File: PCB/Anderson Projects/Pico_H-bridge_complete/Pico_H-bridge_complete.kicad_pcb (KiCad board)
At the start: 4 copper layers, 103.4 x 65.5 mm, 85 parts, among them J1 Screw_Terminal_01x10, J2 Motor Connector, J3 Screw_Terminal_01x02, Q1 AO3400A, Q2 AO3400A, Q3 DMP3130LQ-7, Q4 DMP3130LQ-7, Q5 MMBT3904, Q6 MMBT3904, SW1 SW_DIP_x01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

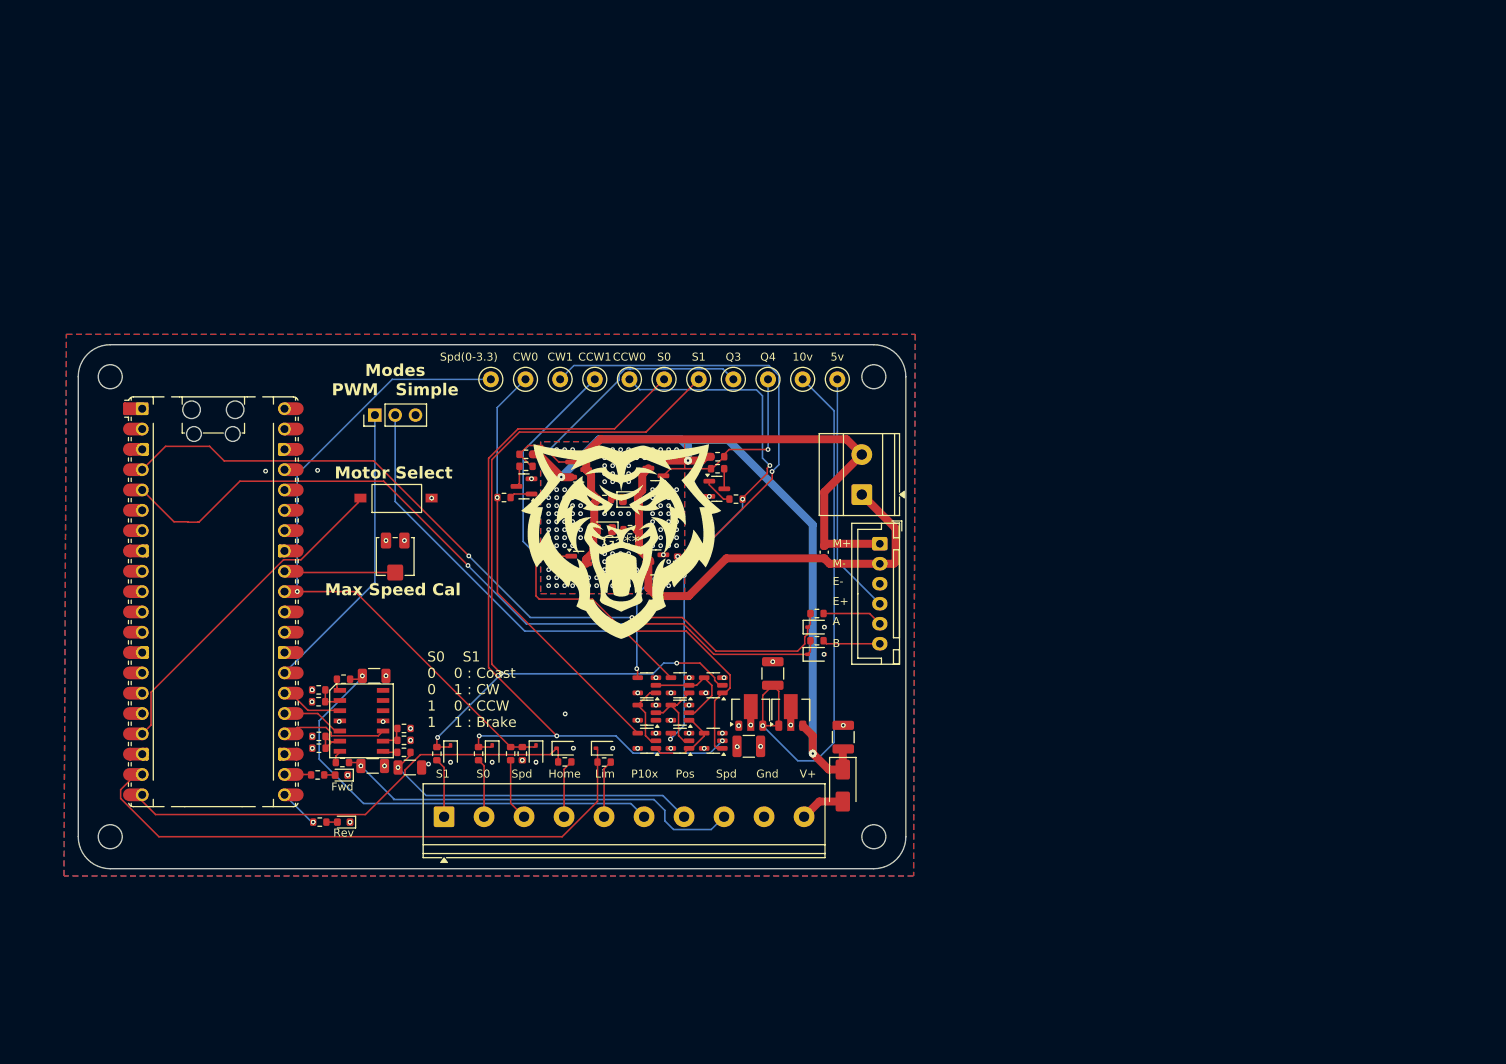
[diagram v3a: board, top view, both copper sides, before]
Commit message: Final Board version prior to testing motor with pulleys. This version would not turn the motor when connected to a generator. The Vgs values for Mosfets needed increased to 10v. Other improvements to make include removing braking functionality to simplify control to Fwd/Rev vice S0/S1.
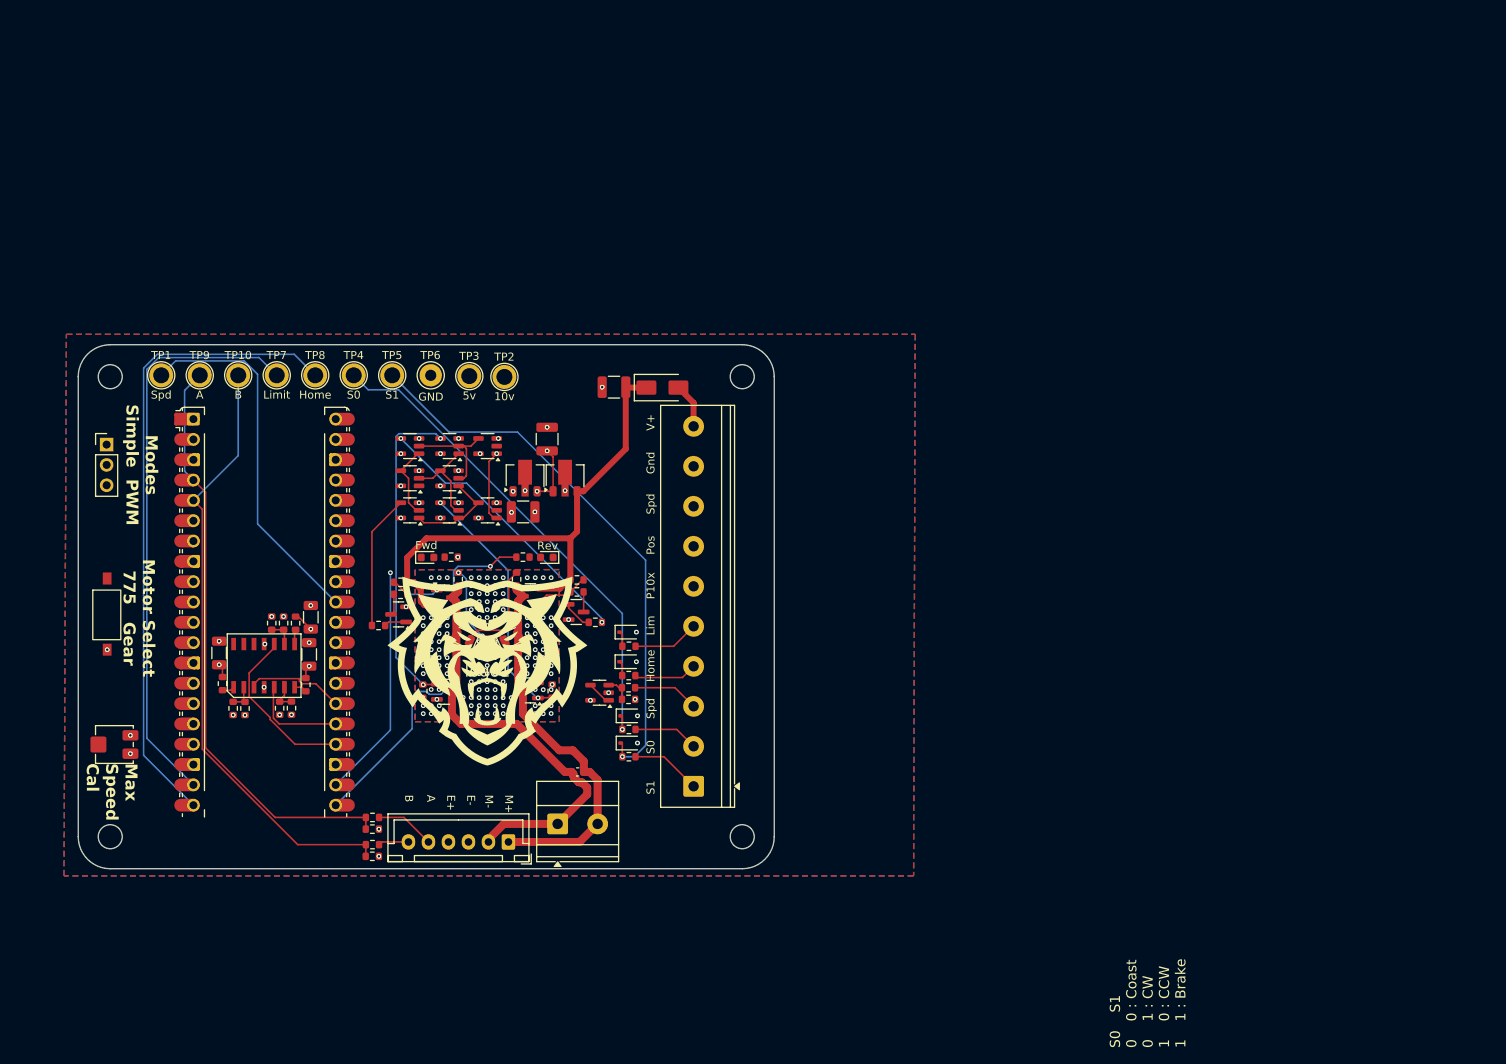
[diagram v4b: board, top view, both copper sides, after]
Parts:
- removed D11, D12, D13, D16, D17: 3.3v, Diode_SMD:D_SOD-323
- removed G***: LOGO, CustomBPA:Bengal_25_25
- removed G***: LOGO, CustomBPA:Bengal_50_50
- removed TP11: CCW1, TestPoint:TestPoint_Loop_D2.50mm_Drill1.0mm
- added D6: 3.3v, Diode_SMD:D_SOD-323, F.Cu at (151.7, 94.6)
- added D7: 3.3v, Diode_SMD:D_SOD-323, F.Cu at (151.7, 90.9)
- added R20: 3.3kΩ, Resistor_SMD:R_0603_1608Metric, F.Cu at (119.8, 119.0)
- added R21: 3.3kΩ, Resistor_SMD:R_0603_1608Metric, F.Cu at (119.8, 115.5)
- added U11: MCP6001R, Package_TO_SOT_SMD:SOT-23-5, F.Cu at (148.2, 98.5)
- added logo1: LOGO, CustomBPA:Bengal_25_25(negative), F.Cu at (134.1, 95.8)
- D1: value LED -> LED_R
- D14, D15: value 3.3v -> 5.1V
- D2: value LED -> LED_W
- D3, D4: value LED -> LED_G
- R10, R4, R6, R8: value 10k -> 3.9k
- R3, R5: value 10k -> 1.8kΩ
- R7, R9: value 1k -> 2.7k
- RV1: value 10k -> 10k pot
- TP1: value Spd(0-3.3) -> Spd; footprint TestPoint:TestPoint_Loop_D2.50mm_Drill1.0mm -> TestPoint:TestPoint_Plated_Hole_D2.0mm
- TP10: value CW0 -> B; footprint TestPoint:TestPoint_Loop_D2.50mm_Drill1.0mm -> TestPoint:TestPoint_Plated_Hole_D2.0mm
- TP2, TP3, TP4, TP5: footprint TestPoint:TestPoint_Loop_D2.50mm_Drill1.0mm -> TestPoint:TestPoint_Plated_Hole_D2.0mm
- TP6: value Q3 -> GND; footprint TestPoint:TestPoint_Loop_D2.50mm_Drill1.0mm -> TestPoint:TestPoint_Loop_D2.60mm_Drill1.4mm_Beaded
- TP7: value Q4 -> Limit; footprint TestPoint:TestPoint_Loop_D2.50mm_Drill1.0mm -> TestPoint:TestPoint_Plated_Hole_D2.0mm
- TP8: value CCW0 -> Home; footprint TestPoint:TestPoint_Loop_D2.50mm_Drill1.0mm -> TestPoint:TestPoint_Plated_Hole_D2.0mm
- TP9: value CW1 -> A; footprint TestPoint:TestPoint_Loop_D2.50mm_Drill1.0mm -> TestPoint:TestPoint_Plated_Hole_D2.0mm
- moved TP7 61.4 mm to (107.8, 58.8)
- moved R3 61.1 mm to (119.8, 114.1)
- moved R5 61.1 mm to (119.8, 117.5)
- moved J2 59.5 mm to (136.8, 117.2), turned to 180 degrees
- moved J3 56.0 mm to (142.9, 114.9), turned to 0 degrees
- moved D5 54.6 mm to (156.0, 60.4), turned to 0 degrees
- moved C4 52.3 mm to (150.0, 60.3), turned to 180 degrees
- moved TP3 46.0 mm to (131.9, 58.9)
- moved TP9 45.1 mm to (98.2, 58.8)
- moved RV1 42.2 mm to (87.5, 105.0), turned to -90 degrees
- moved U3 42.1 mm to (124.5, 67.7)
- moved R1 41.7 mm to (138.6, 81.6)
- moved D1 41.7 mm to (141.6, 81.6)
- moved U10 41.7 mm to (124.5, 71.7)
- moved U12 41.5 mm to (129.4, 67.7)
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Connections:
- C5 pad 1: M+ -> M-
- C5 pad 2: M- -> M+
- D3 pad 2: M+ -> M-
- D4 pad 2: M- -> M+
- Q1 pad 3: M+ -> M-
- Q2 pad 3: M- -> M+
- Q3 pad 3: M+ -> M-
- Q4 pad 3: M- -> M+
- R24 pad 1: Net-(J1-Pin_3) -> GND
- R24 pad 2: Speed_set -> Net-(U11-+)
- R25 pad 1: Speed_set -> Net-(U11-+)
- R25 pad 2: GND -> Net-(J1-Pin_3)
- R7 pad 2: M+ -> M-
- R9 pad 1: Net-(D3-K) -> M+
- R9 pad 2: M- -> Net-(D3-K)
- TP10 pad 1: /H-Bridge/CW0 -> B
- TP6 pad 1: Net-(Q3-G) -> GND
- TP7 pad 1: Net-(Q4-G) -> Limit Switch
- TP8 pad 1: /H-Bridge/CCW0 -> Home
- TP9 pad 1: /H-Bridge/CW1 -> A
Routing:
- net +10V: track 133.2 -> 64.0 mm, vias 2 -> 3
- net /H-Bridge/CW1: track 83.3 -> 31.4 mm, vias 3 -> 2
- net Net-(U1-GPIO13): track 41.8 -> 0.00 mm
- net Net-(U1-GPIO16): track 4.64 -> 46.1 mm
- net S0: track 99.4 -> 62.2 mm, vias 3 -> 1
- net Speed_set PWM: track 36.9 -> 0.00 mm
- net /H-Bridge/CW0: track 53.0 -> 16.8 mm, vias 1 -> 0
- net Net-(U1-GPIO17): track 2.55 -> 38.6 mm, vias 0 -> 2
- net Speed_set: track 82.5 -> 49.1 mm, vias 1 -> 0
- net Net-(Q3-G): track 38.4 -> 6.22 mm, vias 1 -> 2
- net S1: track 101.1 -> 69.7 mm, vias 3 -> 1
- net +Vsup: track 92.6 -> 64.8 mm, vias 3 -> 0
- net /H-Bridge/CCW0: track 61.6 -> 34.9 mm, vias 3 -> 2
- net +5V: track 30.3 -> 56.5 mm
- net A: track 99.1 -> 73.5 mm, vias 2 -> 0
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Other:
- board size 103.4 x 65.5 mm -> 87 x 65.5 mm
- board text added: "Modes Simple PWM"
- board text added: "Motor Select 775 Gear"
- board text added: "PLC Motor Interface Board Anderson - rev1 July 2025"
- board text removed: "Modes PWM Simple"
- board text removed: "Motor Select"
- board text removed: "PLC Motor Interface Board Anderson - rev0 June 2025"

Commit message: Gerber files for Pico_H-bridge_complete v1 generated
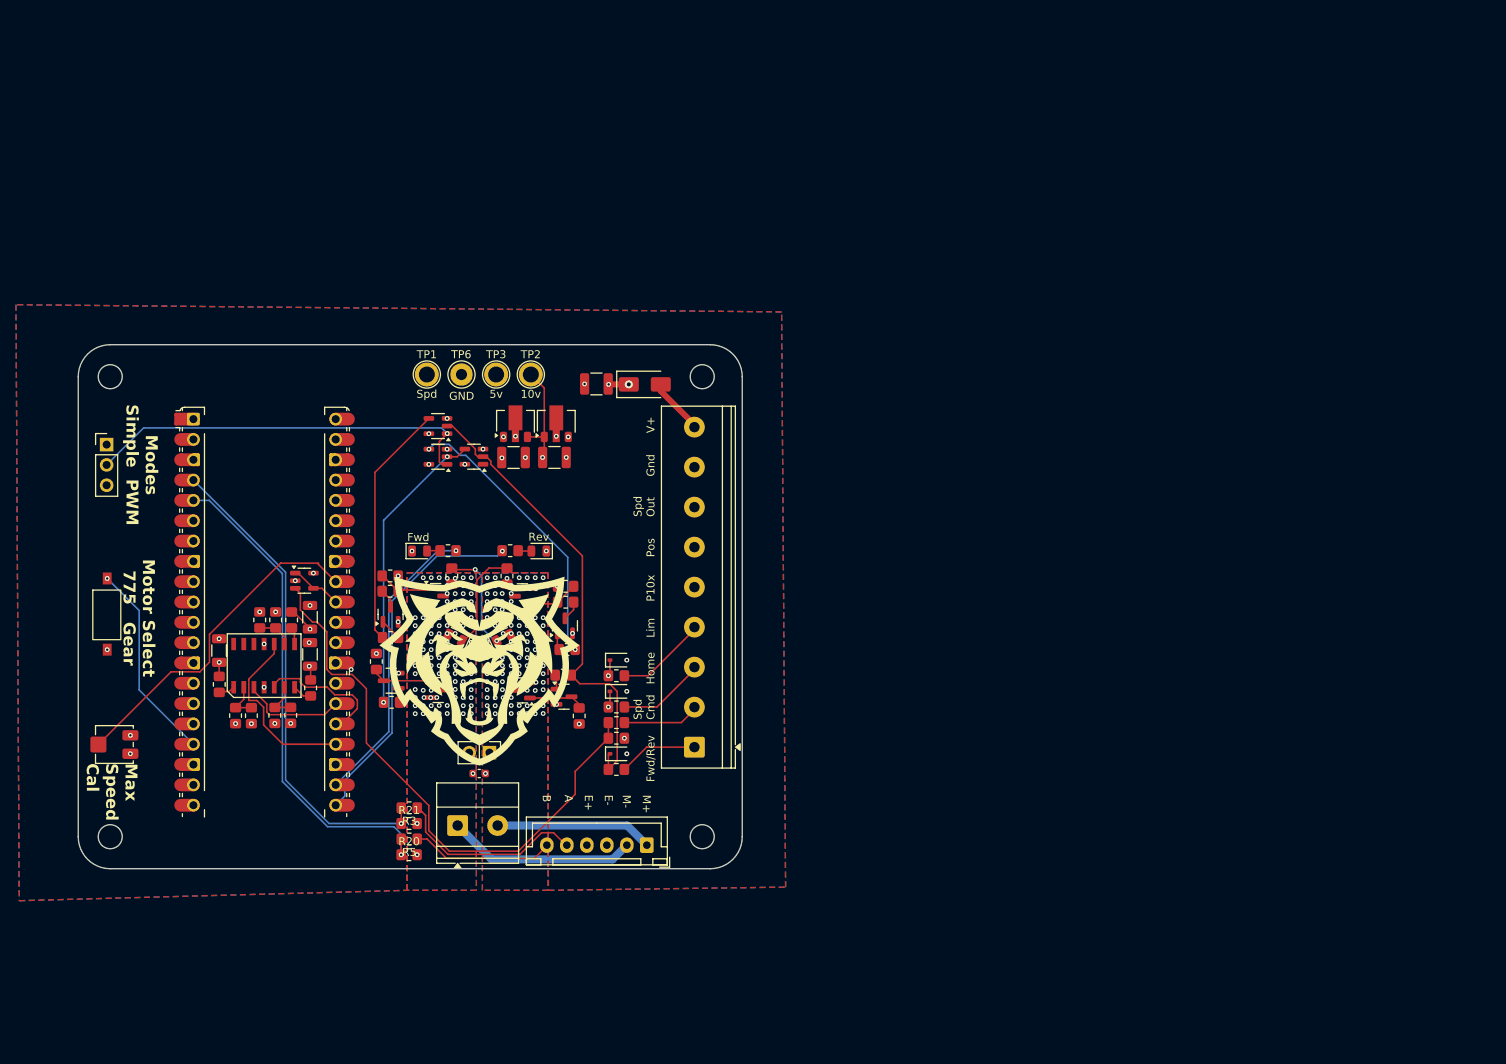
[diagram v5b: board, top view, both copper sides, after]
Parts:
- removed D15: 5.1V, Diode_SMD:D_SOD-323
- removed R37: 10k, Resistor_SMD:R_0603_1608Metric
- removed TP10: B, TestPoint:TestPoint_Plated_Hole_D2.0mm
- removed TP4: S0, TestPoint:TestPoint_Plated_Hole_D2.0mm
- removed TP5: S1, TestPoint:TestPoint_Plated_Hole_D2.0mm
- removed TP7: Limit, TestPoint:TestPoint_Plated_Hole_D2.0mm
- removed TP8: Home, TestPoint:TestPoint_Plated_Hole_D2.0mm
- removed TP9: A, TestPoint:TestPoint_Plated_Hole_D2.0mm
- removed U12, U13: SN74LVC1G32, Package_TO_SOT_SMD:SOT-23-5
- removed U2, U3, U4: 74LVC1G08GV, Package_TO_SOT_SMD:SOT-23-5
- added J4: 2.54 header, Connector_PinHeader_2.54mm:PinHeader_1x02_P2.54mm_Vertical, F.Cu at (134.4, 106.0)
- added Q7: MMBT3904, Package_TO_SOT_SMD:SOT-23, F.Cu at (122.1, 97.0)
- added Q8: MMBT3904, Package_TO_SOT_SMD:SOT-23, F.Cu at (143.7, 99.0)
- added R22: 150Ω, Resistor_SMD:R_0805_2012Metric_Pad1.20x1.40mm_HandSolder, F.Cu at (143.9, 87.2)
- added R23: 1kΩ, Resistor_SMD:R_0805_2012Metric_Pad1.20x1.40mm_HandSolder, F.Cu at (143.9, 85.2)
- D1, D2: footprint LED_SMD:LED_0603_1608Metric -> LED_SMD:LED_0805_2012Metric
- J1: value Screw_Terminal_01x10 -> Screw_Terminal_01x9; footprint TerminalBlock_Phoenix:TerminalBlock_Phoenix_PT-1,5-10-5.0-H_1x10_P5.00mm_Horizontal -> TerminalBlock_Phoenix:TerminalBlock_Phoenix_PT-1,5-9-5.0-H_1x09_P5.00mm_Horizontal
- R1, R10, R11, R12, R13, R14, R15, R16, R17, R18, R19, R2, R20, R21, R24, R25, R3, R35, R4, R5, R6, R7, R9: footprint Resistor_SMD:R_0603_1608Metric -> Resistor_SMD:R_0805_2012Metric_Pad1.20x1.40mm_HandSolder
- R26: value 10k -> 22kΩ; footprint Resistor_SMD:R_0603_1608Metric -> Resistor_SMD:R_0805_2012Metric_Pad1.20x1.40mm_HandSolder
- R27, R31: value 110kΩ -> 22kΩ; footprint Resistor_SMD:R_0603_1608Metric -> Resistor_SMD:R_0805_2012Metric_Pad1.20x1.40mm_HandSolder
- R28: value 2.2kΩ -> 10k; footprint Resistor_SMD:R_0603_1608Metric -> Resistor_SMD:R_0805_2012Metric_Pad1.20x1.40mm_HandSolder
- R29: value 10k -> 150Ω; footprint Resistor_SMD:R_0603_1608Metric -> Resistor_SMD:R_0805_2012Metric_Pad1.20x1.40mm_HandSolder
- R30: value 2.2kΩ -> 1kΩ; footprint Resistor_SMD:R_0603_1608Metric -> Resistor_SMD:R_0805_2012Metric_Pad1.20x1.40mm_HandSolder
- R8: value 3.9k -> 22kΩ; footprint Resistor_SMD:R_0603_1608Metric -> Resistor_SMD:R_0805_2012Metric_Pad1.20x1.40mm_HandSolder
- moved U11 39.5 mm to (111.3, 84.5), turned to 0 degrees
- moved TP1 33.2 mm to (126.6, 58.7)
- moved R26 27.0 mm to (122.2, 99.7)
- moved J2 17.3 mm to (154.1, 117.6)
- moved R28 17.0 mm to (145.6, 101.4), turned to 90 degrees
- moved R8 15.5 mm to (144.1, 93.1), turned to 0 degrees
- moved J3 12.5 mm to (130.4, 115.1)
- moved C5 12.3 mm to (133.1, 108.6)
- moved U8 9.13 mm to (128.0, 69.0)
- moved U10 8.44 mm to (132.5, 69.0)
- moved R27 7.73 mm to (143.6, 96.3), turned to 180 degrees
- moved C12 6.91 mm to (137.4, 69.1)
- moved U7 6.91 mm to (137.7, 64.6)
- moved U6 6.89 mm to (142.8, 64.6)
- moved R35 6.88 mm to (120.3, 94.6)
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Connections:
- C4 pad 1: +Vsup -> +12V
- D14 pad 1: S0 -> Fwd/Rev
- D5 pad 1: +Vsup -> +12V
- J1 pad 5: Net-(J1-Pin_5) -> Analog Position x10
- J1 pad 6: Analog Position x10 -> Analog Position
- J1 pad 7: Analog Position -> Analog Speed
- J1 pad 8: Analog Speed -> GND
- J1 pad 9: GND -> Net-(D5-A)
- Q1 pad 1: /H-Bridge/CCW1 -> Net-(Q1-G)
- Q2 pad 1: /H-Bridge/CW1 -> Net-(Q2-G)
- Q3 pad 2: +Vsup -> +12V
- Q4 pad 2: +Vsup -> +12V
- R10 pad 1: Net-(J1-Pin_2) -> Net-(J1-Pin_1)
- R10 pad 2: S0 -> Fwd/Rev
- R25 pad 2: Net-(J1-Pin_3) -> Net-(J1-Pin_2)
- R26 pad 1: Net-(Q4-G) -> /H-Bridge/CCW1
- R26 pad 2: Net-(Q6-C) -> Net-(Q7-B)
- R27 pad 1: Net-(Q6-B) -> Fwd/Rev
- R27 pad 2: /H-Bridge/CCW0 -> Net-(Q8-B)
- R28 pad 1: +Vsup -> +10V
- R28 pad 2: Net-(Q4-G) -> Net-(Q2-G)
- R30 pad 2: +Vsup -> +12V
- R35 pad 1: /H-Bridge/CCW1 -> +10V
- R35 pad 2: GND -> Net-(Q1-G)
- R4 pad 1: Net-(J1-Pin_4) -> Net-(J1-Pin_3)
- R6 pad 1: Net-(J1-Pin_5) -> Net-(J1-Pin_4)
- R8 pad 1: Net-(J1-Pin_1) -> Net-(Q6-B)
- R8 pad 2: S1 -> /H-Bridge/CCW0
- U10 pad 2: Net-(U10-Pad2) -> Fwd/Rev
- U10 pad 4: Net-(U10-Pad4) -> /H-Bridge/CCW1
- U6 pad 3: +Vsup -> +12V
- U8 pad 2: S0 -> /H-Bridge/CCW1
- U8 pad 4: Net-(U13-Pad1) -> /H-Bridge/CCW0
- U9 pad 2: S1 -> Fwd/Rev
- U9 pad 4: Net-(U12-Pad2) -> /H-Bridge/CW0
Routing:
- net S1: track 69.7 -> 0.00 mm, vias 1 -> 0
- net Net-(U11-+): track 3.25 -> 72.0 mm
- net +Vsup: track 64.8 -> 0.00 mm
- net S0: track 62.2 -> 0.00 mm, vias 1 -> 0
- net Fwd/Rev: track 0.00 -> 58.6 mm
- net Speed_set PWM: track 0.00 -> 51.5 mm
- net +10V: track 64.0 -> 107.6 mm, vias 3 -> 4
- net Net-(U1-GPIO27_ADC1): track 0.00 -> 42.2 mm
- net /H-Bridge/CW1: track 31.4 -> 0.00 mm, vias 2 -> 0
- net M-: track 53.6 -> 23.6 mm, vias 0 -> 114
- net M+: track 47.9 -> 19.7 mm, vias 0 -> 115
- net Net-(U1-GPIO13): track 0.00 -> 25.2 mm, vias 0 -> 1
- net Home: track 82.3 -> 59.0 mm, vias 0 -> 1
- net Analog Speed: track 58.0 -> 77.6 mm
- net Net-(J2-Pin_5): track 7.44 -> 23.9 mm
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- added copper zone on In1.Cu, net +12V
- added copper zone on B.Cu, net M+
- added copper zone on F.Cu, net M+
- added copper zone on B.Cu, net M-
- added copper zone on F.Cu, net M-
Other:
- board size 87 x 65.5 mm -> 83 x 65.5 mm
- board text added: "Fwd/Rev"
- board text added: "Spd Cmd"
- board text added: "Spd Out"
- board text removed: "S0"
- board text removed: "S0 S1 0 0 : Coast 0 1 : CW 1 0 : CCW 1 1 : Brake"
- board text removed: "S1"
- board text removed: "Spd"
